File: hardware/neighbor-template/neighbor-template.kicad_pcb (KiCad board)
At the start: 4 copper layers, 70.7 x 53.3 mm, 7 parts, among them J1 NEIGHBOR1, J2 NEIGHBOR2, J7 BONUS_ROW

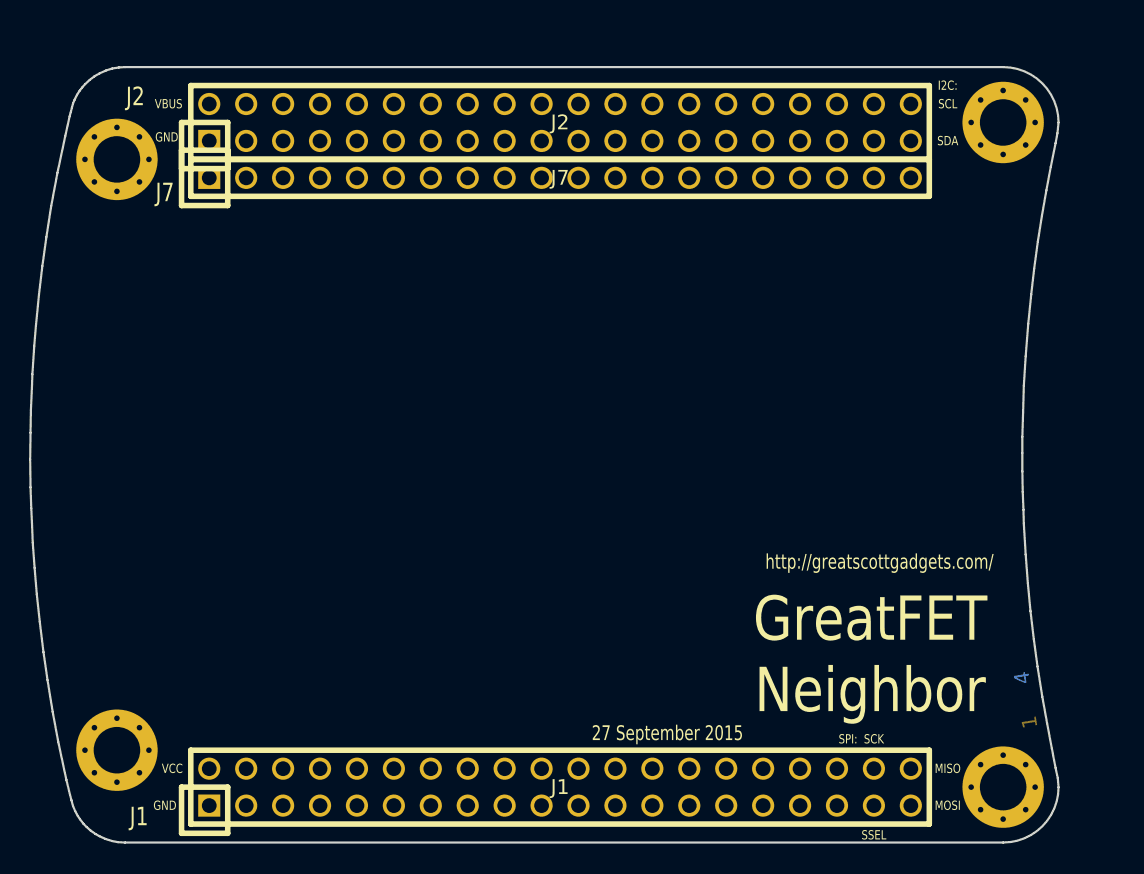
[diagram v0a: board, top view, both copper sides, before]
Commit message: begonia: extended spring pin PCB edge for fit into IM-Me battery compartment
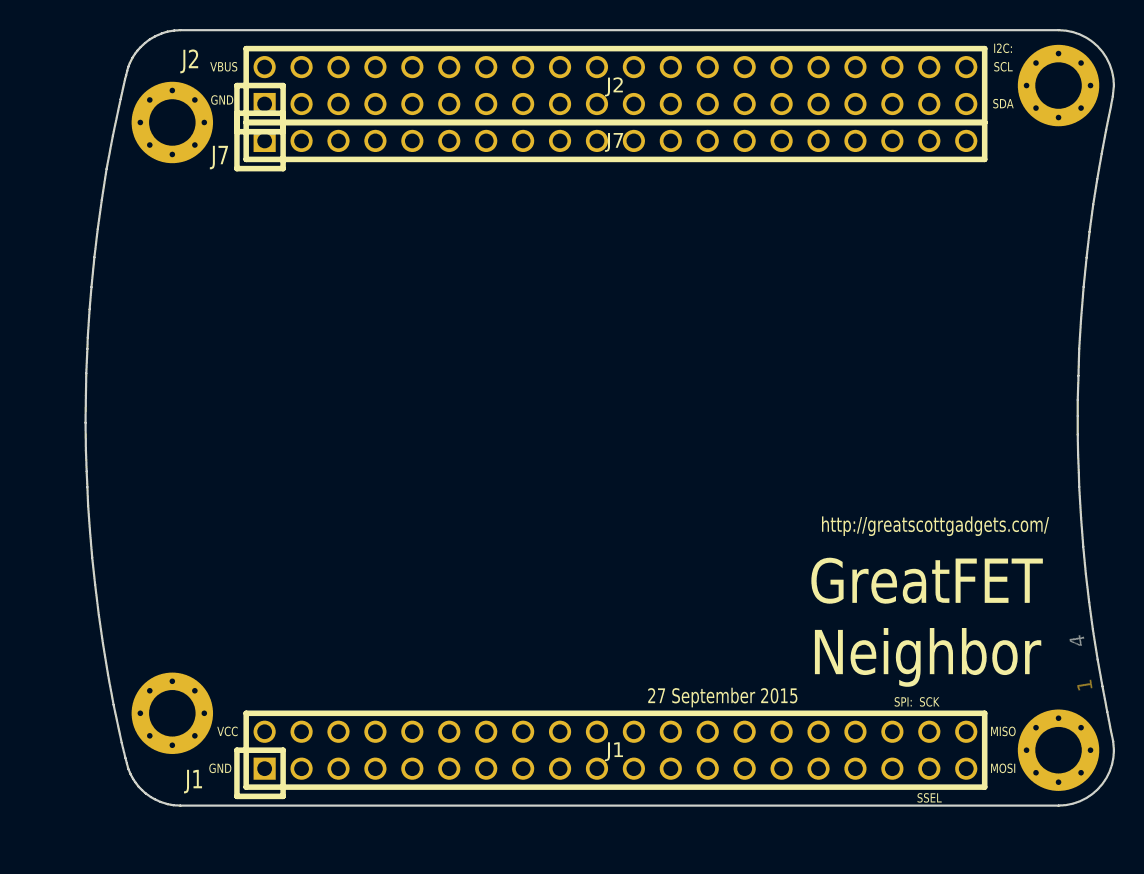
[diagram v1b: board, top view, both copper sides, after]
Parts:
- moved J1 4.58 mm to (146.1, 118.1)
- moved J2 4.58 mm to (146.1, 72.4)
- moved MH3 4.58 mm to (176.5, 118.1)
- moved MH4 4.58 mm to (176.5, 72.4)
- moved J7 4.58 mm to (146.1, 76.2)
- moved MH2 4.58 mm to (115.6, 115.6)
- moved MH1 4.58 mm to (115.6, 74.9)
